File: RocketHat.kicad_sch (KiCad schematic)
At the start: 23 parts, among them J1 Screw_Terminal_01x02, J10 Raspberry_Pi_2_3, J2 Conn_01x06_Female, J3 Conn_01x06_Female, J4 Conn_01x07_Female, J5 Conn_01x06_Female, J6 Conn_01x04_Female, J7 Conn_01x10_Female, J8 Conn_01x02, J9 Conn_01x10_Female, Q1 FQP27P06, U1 CAT24C128

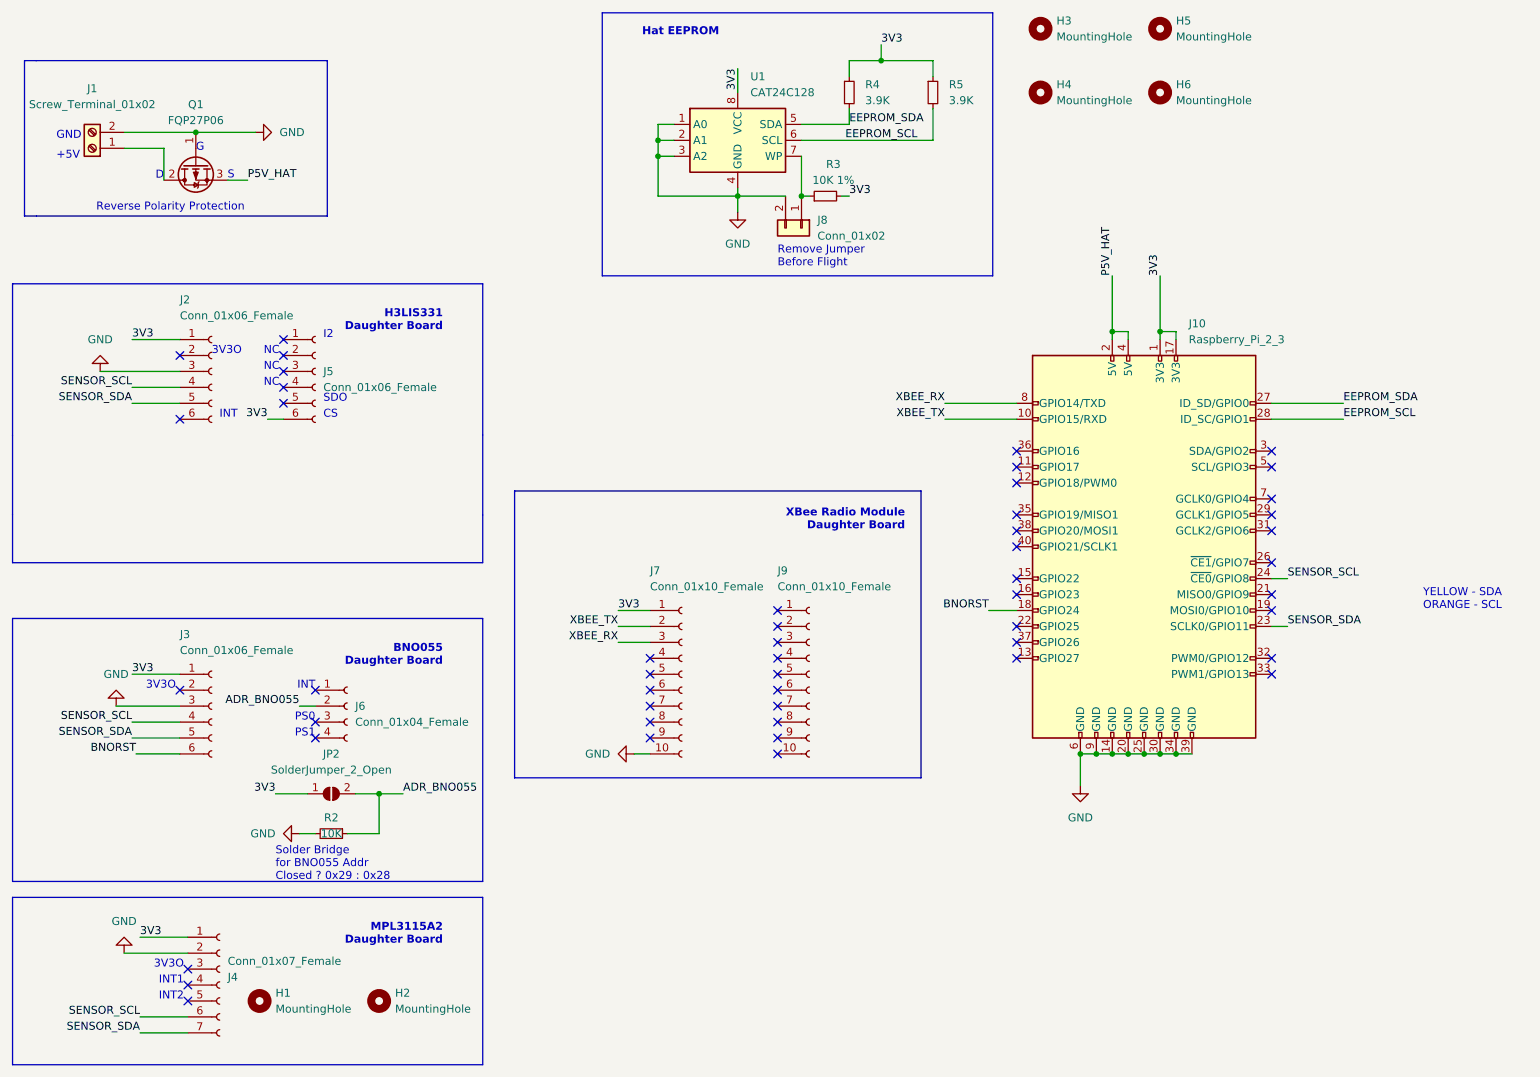
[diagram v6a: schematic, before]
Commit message: Fixed Inverted Layout
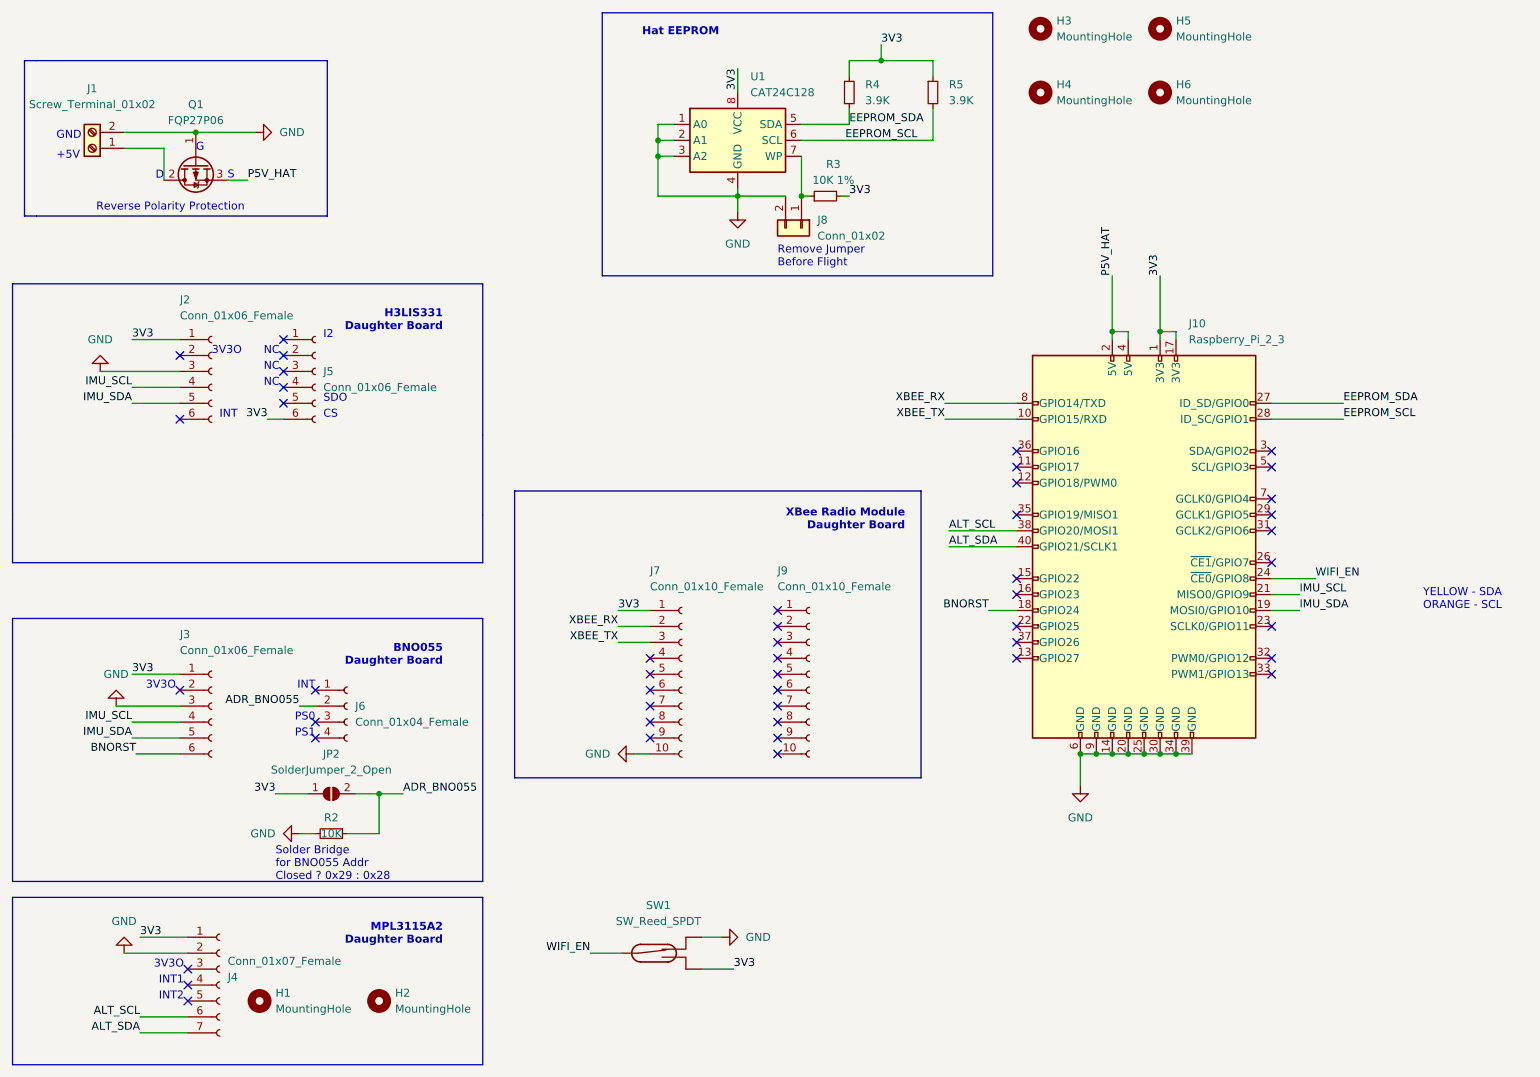
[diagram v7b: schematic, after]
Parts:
- added SW1: SW_Reed_SPDT, Button_Switch_THT:KSA_Tactile_SPST, symbol Switch:SW_Reed_SPDT
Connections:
- net 3V3: now also SW1.3
- net GND: now also SW1.1
- net XBEE_RX: now also J7.2 (Pin_2); no longer J7.3 (Pin_3)
- net XBEE_TX: now also J7.3 (Pin_3); no longer J7.2 (Pin_2)
- net IMU_SDA: now reaches J10.19 (MOSI0/GPIO10)
- net IMU_SDA: now also J2.5 (Pin_5), J3.5 (Pin_5)
- net IMU_SCL: now reaches J10.21 (MISO0/GPIO9)
- net IMU_SCL: now also J2.4 (Pin_4), J3.4 (Pin_4)
- net ALT_SCL: now reaches J10.38 (GPIO20/MOSI1)
- net ALT_SCL: now also J4.6 (Pin_6)
- net ALT_SDA: now reaches J10.40 (GPIO21/SCLK1)
- net ALT_SDA: now also J4.7 (Pin_7)
- removed net SENSOR_SCL: J10.24 (~{CE0}/GPIO8), J2.4 (Pin_4), J3.4 (Pin_4), J4.6 (Pin_6)
- removed net SENSOR_SDA: J10.23 (SCLK0/GPIO11), J2.5 (Pin_5), J3.5 (Pin_5), J4.7 (Pin_7)
- new net WIFI_EN: J10.24 (~{CE0}/GPIO8), SW1.2
- no-connect marks 51 -> 48
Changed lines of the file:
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@@
   (no_connect (at 134.62 132.08))
   (no_connect (at 134.62 124.46))
-  (no_connect (at 193.04 109.22))
   (no_connect (at 134.62 129.54))
   (no_connect (at 76.2 81.28))
+  (no_connect (at 193.04 109.22))
   (no_connect (at 154.94 127))
   (no_connect (at 134.62 134.62))
   (no_connect (at 59.69 73.66))
+  (no_connect (at 233.68 116.84))
   (no_connect (at 233.68 124.46))
   (no_connect (at 233.68 121.92))
-  (no_connect (at 233.68 114.3))
-  (no_connect (at 233.68 111.76))
   (no_connect (at 233.68 106.68))
   (no_connect (at 233.68 101.6))
@@
   (no_connect (at 193.04 93.98))
   (no_connect (at 193.04 99.06))
-  (no_connect (at 193.04 101.6))
-  (no_connect (at 193.04 104.14))
-  (no_connect (at 193.04 111.76))
   (no_connect (at 193.04 116.84))
   (no_connect (at 193.04 119.38))
@@
   (no_connect (at 81.28 132.08))
   (no_connect (at 154.94 119.38))
+  (no_connect (at 193.04 111.76))
   (no_connect (at 60.96 171.45))
   (no_connect (at 154.94 114.3))
@@
     (stroke (width 0) (type default) (color 0 0 0 0))
   )
+  (wire (pts (xy 129.54 119.38) (xy 134.62 119.38))
+    (stroke (width 0) (type default) (color 0 0 0 0))
+  )
   (polyline (pts (xy 127 19.05) (xy 189.23 19.05))
     (stroke (width 0) (type default) (color 0 0 0 0))
@@
     (stroke (width 0) (type default) (color 0 0 0 0))
   )
-  (wire (pts (xy 233.68 109.22) (xy 236.22 109.22))
-    (stroke (width 0) (type default) (color 0 0 0 0))
-  )
   (wire (pts (xy 74.93 143.51) (xy 80.01 143.51))
     (stroke (width 0) (type default) (color 0 0 0 0))
@@
     (stroke (width 0) (type default) (color 0 0 0 0))
   )
+  (wire (pts (xy 233.68 111.76) (xy 238.125 111.76))
+    (stroke (width 0) (type default) (color 0 0 0 0))
+  )
   (polyline (pts (xy 33.02 160.02) (xy 33.02 186.69))
     (stroke (width 0) (type default) (color 0 0 0 0))
@@
     (stroke (width 0) (type default) (color 0 0 0 0))
   )
+  (wire (pts (xy 182.245 104.14) (xy 193.04 104.14))
+    (stroke (width 0) (type default) (color 0 0 0 0))
+  )
+  (wire (pts (xy 233.68 114.3) (xy 238.125 114.3))
+    (stroke (width 0) (type default) (color 0 0 0 0))
+  )
+  (wire (pts (xy 125.095 168.91) (xy 130.175 168.91))
+    (stroke (width 0) (type default) (color 0 0 0 0))
+  )
   (wire (pts (xy 53.34 181.61) (xy 60.96 181.61))
     (stroke (width 0) (type default) (color 0 0 0 0))
@@
     (stroke (width 0) (type default) (color 0 0 0 0))
   )
-  (wire (pts (xy 129.54 119.38) (xy 134.62 119.38))
-    (stroke (width 0) (type default) (color 0 0 0 0))
-  )
   (wire (pts (xy 135.89 36.83) (xy 135.89 39.37))
     (stroke (width 0) (type default) (color 0 0 0 0))
@@
     (stroke (width 0) (type default) (color 0 0 0 0))
   )
-  (wire (pts (xy 233.68 116.84) (xy 236.22 116.84))
-    (stroke (width 0) (type default) (color 0 0 0 0))
-  )
   (polyline (pts (xy 33.02 62.23) (xy 33.02 86.36))
     (stroke (width 0) (type default) (color 0 0 0 0))
   )
+  (wire (pts (xy 142.875 171.45) (xy 147.955 171.45))
+    (stroke (width 0) (type default) (color 0 0 0 0))
+  )
   (wire (pts (xy 210.82 137.16) (xy 213.36 137.16))
     (stroke (width 0) (type default) (color 0 0 0 0))
@@
     (stroke (width 0) (type default) (color 0 0 0 0))
   )
+  (wire (pts (xy 142.875 166.37) (xy 146.05 166.37))
+    (stroke (width 0) (type default) (color 0 0 0 0))
+  )
   (wire (pts (xy 91.44 149.86) (xy 91.44 143.51))
     (stroke (width 0) (type default) (color 0 0 0 0))
@@
     (stroke (width 0) (type default) (color 0 0 0 0))
   )
+  (wire (pts (xy 129.54 116.84) (xy 134.62 116.84))
+    (stroke (width 0) (type default) (color 0 0 0 0))
+  )
   (polyline (pts (xy 33.02 160.02) (xy 107.95 160.02))
     (stroke (width 0) (type default) (color 0 0 0 0))
@@
     (stroke (width 0) (type default) (color 0 0 0 0))
   )
-  (wire (pts (xy 129.54 116.84) (xy 134.62 116.84))
-    (stroke (width 0) (type default) (color 0 0 0 0))
-  )
   (polyline (pts (xy 33.02 99.06) (xy 33.02 106.68))
     (stroke (width 0) (type default) (color 0 0 0 0))
@@
   )
   (wire (pts (xy 135.89 41.91) (xy 138.43 41.91))
+    (stroke (width 0) (type default) (color 0 0 0 0))
+  )
+  (wire (pts (xy 182.245 101.6) (xy 193.04 101.6))
+    (stroke (width 0) (type default) (color 0 0 0 0))
+  )
+  (wire (pts (xy 233.68 109.22) (xy 240.665 109.22))
     (stroke (width 0) (type default) (color 0 0 0 0))
   )
@@
     (effects (font (size 1.27 1.27)) (justify right bottom))
   )
+  (label "IMU_SCL" (at 238.125 111.76 0)
+    (effects (font (size 1.27 1.27)) (justify left bottom))
+  )
   (label "BNORST" (at 52.705 137.16 180)
     (effects (font (size 1.27 1.27)) (justify right bottom))
   )
-  (label "SENSOR_SCL" (at 52.07 132.08 180)
-    (effects (font (size 1.27 1.27)) (justify right bottom))
-  )
-  (label "SENSOR_SDA" (at 52.07 134.62 180)
+  (label "IMU_SCL" (at 52.07 132.08 180)
+    (effects (font (size 1.27 1.27)) (justify right bottom))
+  )
+  (label "IMU_SDA" (at 52.07 134.62 180)
     (effects (font (size 1.27 1.27)) (justify right bottom))
   )
@@
     (effects (font (size 1.27 1.27)) (justify left bottom))
   )
-  (label "SENSOR_SCL" (at 53.34 179.07 180)
-    (effects (font (size 1.27 1.27)) (justify right bottom))
+  (label "ALT_SCL" (at 53.34 179.07 180)
+    (effects (font (size 1.27 1.27)) (justify right bottom))
+  )
+  (label "IMU_SDA" (at 238.125 114.3 0)
+    (effects (font (size 1.27 1.27)) (justify left bottom))
   )
   (label "EEPROM_SCL" (at 165.735 39.37 0)
@@
     (effects (font (size 1.27 1.27)) (justify left bottom))
   )
-  (label "XBEE_RX" (at 129.54 119.38 180)
+  (label "XBEE_RX" (at 129.54 116.84 180)
     (effects (font (size 1.27 1.27)) (justify right bottom))
   )
@@
     (effects (font (size 1.27 1.27)) (justify left bottom))
   )
-  (label "SENSOR_SCL" (at 52.07 78.74 180)
-    (effects (font (size 1.27 1.27)) (justify right bottom))
+  (label "IMU_SCL" (at 52.07 78.74 180)
+    (effects (font (size 1.27 1.27)) (justify right bottom))
+  )
+  (label "3V3" (at 147.955 171.45 0)
+    (effects (font (size 1.27 1.27)) (justify left bottom))
   )
   (label "3V3" (at 52.07 124.46 0)
@@
     (effects (font (size 1.27 1.27)) (justify left bottom))
   )
+  (label "ALT_SCL" (at 182.245 101.6 0)
+    (effects (font (size 1.27 1.27)) (justify left bottom))
+  )
+  (label "WIFI_EN" (at 240.665 109.22 0)
+    (effects (font (size 1.27 1.27)) (justify left bottom))
+  )
   (label "XBEE_TX" (at 181.61 83.82 180)
     (effects (font (size 1.27 1.27)) (justify right bottom))
@@
     (effects (font (size 1.27 1.27)) (justify left bottom))
   )
-  (label "XBEE_TX" (at 129.54 116.84 180)
+  (label "XBEE_TX" (at 129.54 119.38 180)
     (effects (font (size 1.27 1.27)) (justify right bottom))
   )
@@
     (effects (font (size 1.27 1.27)) (justify left bottom))
   )
-  (label "SENSOR_SDA" (at 236.22 116.84 0)
-    (effects (font (size 1.27 1.27)) (justify left bottom))
-  )
   (label "3V3" (at 74.93 143.51 180)
     (effects (font (size 1.27 1.27)) (justify right bottom))
   )
-  (label "SENSOR_SDA" (at 52.07 81.28 180)
+  (label "IMU_SDA" (at 52.07 81.28 180)
     (effects (font (size 1.27 1.27)) (justify right bottom))
   )
@@
     (effects (font (size 1.27 1.27)) (justify right bottom))
   )
-  (label "SENSOR_SDA" (at 53.34 181.61 180)
-    (effects (font (size 1.27 1.27)) (justify right bottom))
-  )
-  (label "SENSOR_SCL" (at 236.22 109.22 0)
+  (label "WIFI_EN" (at 125.095 168.91 180)
+    (effects (font (size 1.27 1.27)) (justify right bottom))
+  )
+  (label "ALT_SDA" (at 53.34 181.61 180)
+    (effects (font (size 1.27 1.27)) (justify right bottom))
+  )
+  (label "ALT_SDA" (at 182.245 104.14 0)
     (effects (font (size 1.27 1.27)) (justify left bottom))
   )
@@
     (pin "1")
     (pin "2")
+  )
+  (symbol (lib_id "power:GND") (at 146.05 166.37 90) (unit 1)
+    (in_bom yes) (on_board yes) (fields_autoplaced)
+    (property "Reference" "#PWR0101" (id 0) (at 152.4 166.37 0)
+      (effects (font (size 1.27 1.27)) hide)
+    )
+    (property "Value" "GND" (id 1) (at 149.86 166.3699 90)
+      (effects (font (size 1.27 1.27)) (justify right))
+    )
+    (property "Footprint" "" (id 2) (at 146.05 166.37 0)
+      (effects (font (size 1.27 1.27)) hide)
+    )
+    (property "Datasheet" "" (id 3) (at 146.05 166.37 0)
+      (effects (font (size 1.27 1.27)) hide)
+    )
+    (pin "1")
   )
   (symbol (lib_id "Connector:Raspberry_Pi_2_3") (at 213.36 104.14 0) (unit 1)
@@
     (pin "6")
   )
+  (symbol (lib_id "Switch:SW_Reed_SPDT") (at 135.255 168.91 0) (unit 1)
+    (in_bom yes) (on_board yes) (fields_autoplaced)
+    (property "Reference" "SW1" (id 0) (at 135.9535 161.29 0))
+    (property "Value" "SW_Reed_SPDT" (id 1) (at 135.9535 163.83 0))
+    (property "Footprint" "Button_Switch_THT:KSA_Tactile_SPST" (id 2) (at 135.255 168.91 0)
+      (effects (font (size 1.27 1.27)) hide)
+    )
+    (property "Datasheet" "~" (id 3) (at 135.255 168.91 0)
+      (effects (font (size 1.27 1.27)) hide)
+    )
+    (pin "1")
+    (pin "2")
+    (pin "3")
+  )
   (symbol (lib_id "power:GND") (at 78.74 149.86 270) (unit 1)
     (in_bom yes) (on_board yes) (fields_autoplaced)
@@
       (reference "#PWR09") (unit 1) (value "GND") (footprint "")
     )
+    (path "/1338b916-2b07-4ea8-b40e-f5f3c6b6289c"
+      (reference "#PWR0101") (unit 1) (value "GND") (footprint "")
+    )
     (path "/9745344d-f5a4-4b56-b292-fac7f1ad12d0"
       (reference "H1") (unit 1) (value "MountingHole") (footprint "MountingHole:MountingHole_2.2mm_M2")
@@
       (reference "R5") (unit 1) (value "3.9K") (footprint "Resistor_THT:R_Axial_DIN0204_L3.6mm_D1.6mm_P5.08mm_Horizontal")
     )
+    (path "/d7e14f87-889d-4cc4-a810-86aef18e0af8"
+      (reference "SW1") (unit 1) (value "SW_Reed_SPDT") (footprint "Button_Switch_THT:KSA_Tactile_SPST")
+    )
     (path "/7e172c4b-1dda-4e37-981f-3dc1a6417140"

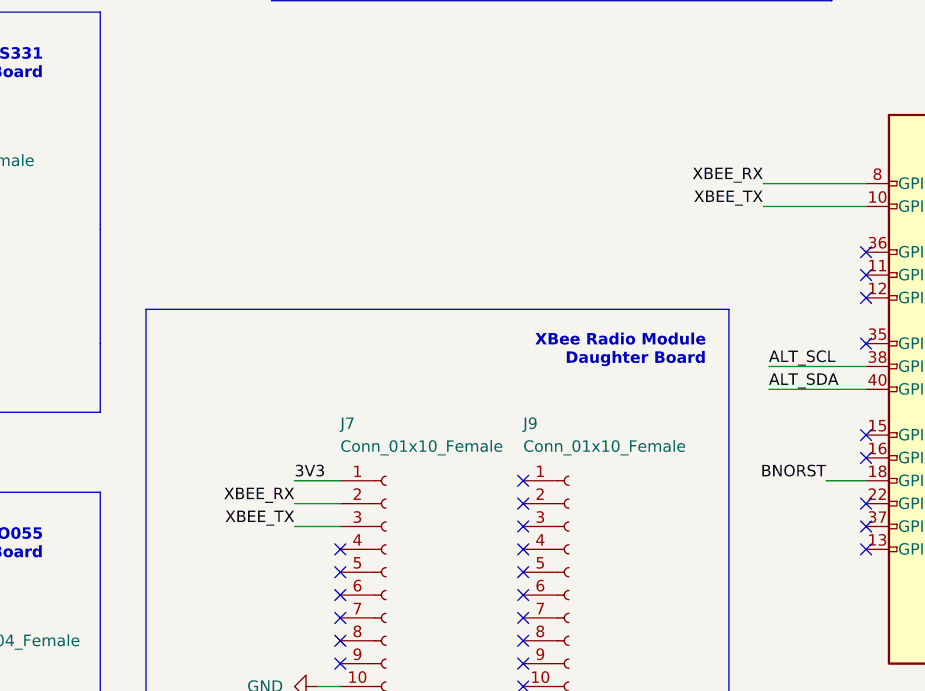
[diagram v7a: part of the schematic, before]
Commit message: Passed DRC With 1.1.1
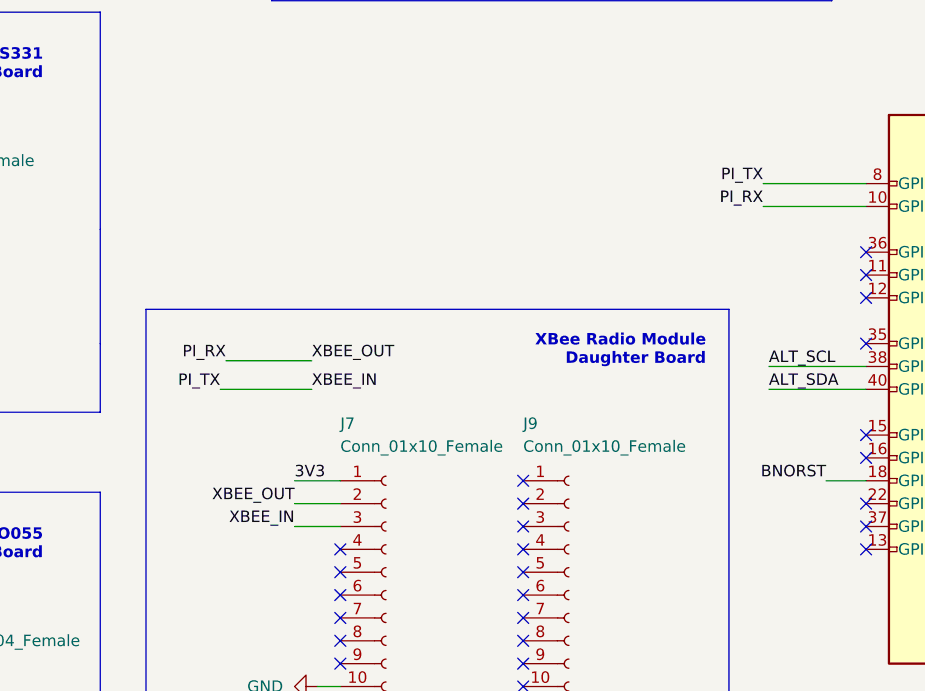
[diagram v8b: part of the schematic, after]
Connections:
- net XBEE_RX renamed PI_RX
- net PI_RX: now also J10.10 (GPIO15/RXD); no longer J10.8 (GPIO14/TXD)
- net XBEE_TX renamed PI_TX
- net PI_TX: now also J10.8 (GPIO14/TXD); no longer J10.10 (GPIO15/RXD)
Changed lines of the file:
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@@
+    (stroke (width 0) (type default) (color 0 0 0 0))
+  )
+  (wire (pts (xy 121.92 100.965) (xy 131.445 100.965))
     (stroke (width 0) (type default) (color 0 0 0 0))
   )
@@
   )
   (wire (pts (xy 91.44 143.51) (xy 95.25 143.51))
+    (stroke (width 0) (type default) (color 0 0 0 0))
+  )
+  (wire (pts (xy 121.285 104.14) (xy 131.445 104.14))
     (stroke (width 0) (type default) (color 0 0 0 0))
   )
@@
     (effects (font (size 1.27 1.27)) (justify left bottom))
   )
+  (label "PI_TX" (at 121.285 104.14 180)
+    (effects (font (size 1.27 1.27)) (justify right bottom))
+  )
   (label "ADR_BNO055" (at 78.74 129.54 180)
     (effects (font (size 1.27 1.27)) (justify right bottom))
@@
     (effects (font (size 1.27 1.27)) (justify left bottom))
   )
-  (label "XBEE_RX" (at 129.54 116.84 180)
+  (label "XBEE_OUT" (at 129.54 116.84 180)
     (effects (font (size 1.27 1.27)) (justify right bottom))
   )
@@
     (effects (font (size 1.27 1.27)) (justify left bottom))
   )
-  (label "XBEE_TX" (at 181.61 83.82 180)
+  (label "PI_RX" (at 181.61 83.82 180)
     (effects (font (size 1.27 1.27)) (justify right bottom))
   )
@@
     (effects (font (size 1.27 1.27)) (justify left bottom))
   )
-  (label "XBEE_RX" (at 181.61 81.28 180)
+  (label "PI_TX" (at 181.61 81.28 180)
     (effects (font (size 1.27 1.27)) (justify right bottom))
   )
@@
     (effects (font (size 1.27 1.27)) (justify left bottom))
   )
-  (label "XBEE_TX" (at 129.54 119.38 180)
+  (label "PI_RX" (at 121.92 100.965 180)
+    (effects (font (size 1.27 1.27)) (justify right bottom))
+  )
+  (label "XBEE_IN" (at 129.54 119.38 180)
     (effects (font (size 1.27 1.27)) (justify right bottom))
   )
@@
     (effects (font (size 1.27 1.27)) (justify left bottom))
   )
+  (label "XBEE_OUT" (at 131.445 100.965 0)
+    (effects (font (size 1.27 1.27)) (justify left bottom))
+  )
+  (label "XBEE_IN" (at 131.445 104.14 0)
+    (effects (font (size 1.27 1.27)) (justify left bottom))
+  )
